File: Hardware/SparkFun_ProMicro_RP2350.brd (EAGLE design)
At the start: 17.8 x 33 mm, 117 parts, among them J2 QWIIC_RIGHT_ANGLE, J5 USB Female Type C Connector, U1 RT9080-33GJ5, U2 RP2350A, U3 WS2812_2020, U4 W25QXX128MBIT, Y1 12MHz

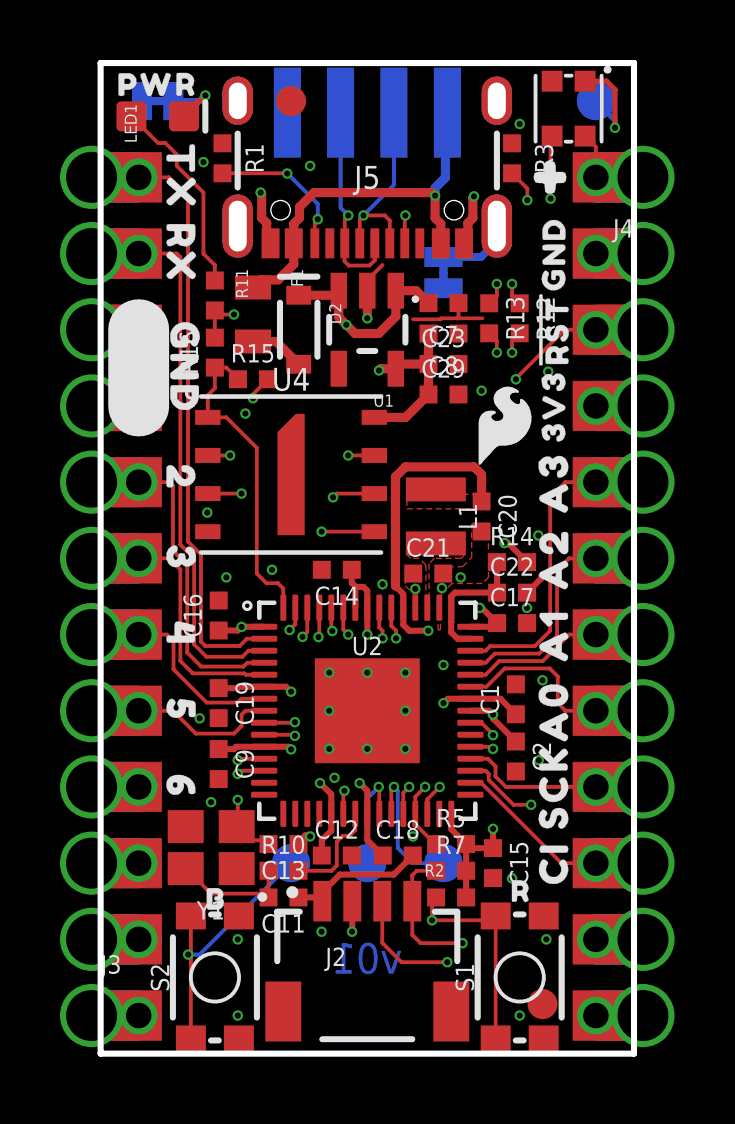
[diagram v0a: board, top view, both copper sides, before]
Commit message: Design review updates
Change all text and labels in schematic to vector font
Fix overlapping text with Qwiic connector in schematic
Add part number to flash memory section title
Fix acid trap on RAW pad
Add more GND vias
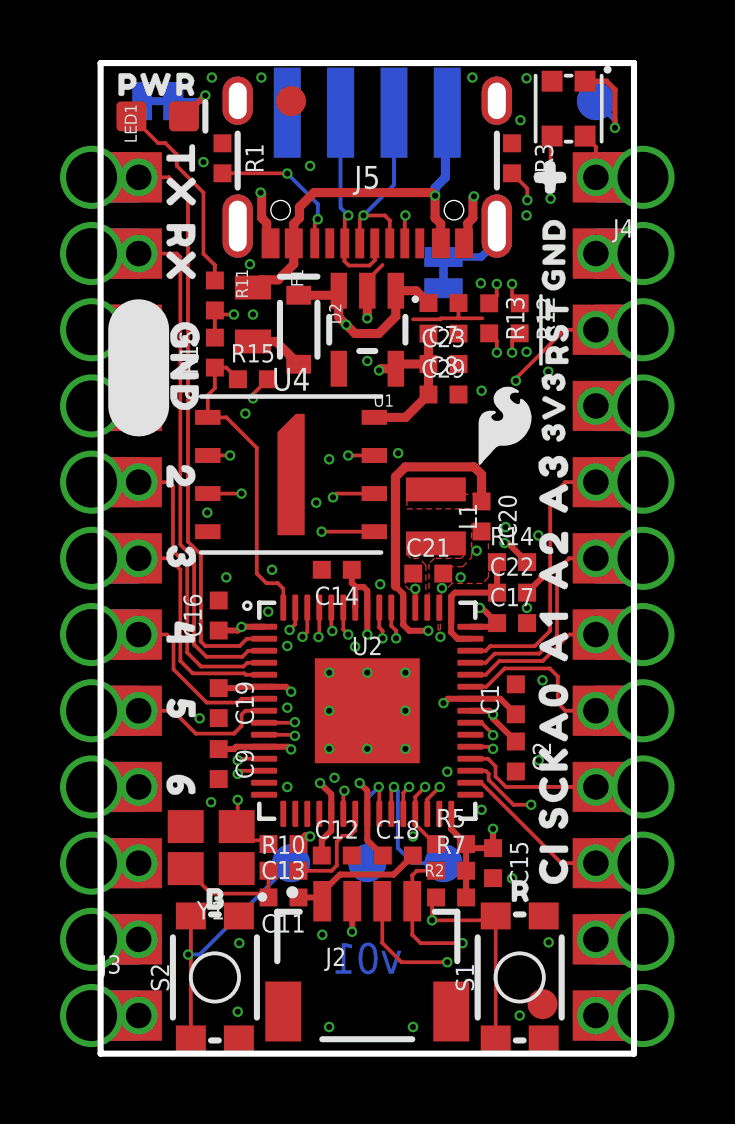
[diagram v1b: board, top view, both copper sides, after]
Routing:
- net GND: vias 39 -> 63
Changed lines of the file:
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@@
 <setting verticaltext="up"/>
 </settings>
-<grid distance="0.05" unitdist="inch" unit="inch" style="lines" multiple="1" display="yes" altdistance="0.005" altunitdist="inch" altunit="inch"/>
+<grid distance="0.05" unitdist="inch" unit="inch" style="lines" multiple="1" display="yes" altdistance="0.001" altunitdist="inch" altunit="inch"/>
 <layers>
 <layer number="1" name="Top" color="4" fill="1" visible="yes" active="yes"/>
@@
 <via x="4.191" y="15.875" extent="1-16" drill="0.2"/>
 <via x="5.715" y="16.129" extent="1-16" drill="0.2"/>
-<via x="9.398" y="15.6464" extent="1-16" drill="0.2"/>
+<via x="9.3218" y="15.6464" extent="1-16" drill="0.2"/>
 <via x="12.0015" y="15.875" extent="1-16" drill="0.2"/>
 <via x="14.9225" y="22.733" extent="1-16" drill="0.2"/>
@@
 <via x="3.429" y="29.718" extent="1-16" drill="0.2"/>
 <via x="6.985" y="29.591" extent="1-16" drill="0.2"/>
-<via x="13.97" y="30.988" extent="1-16" drill="0.2"/>
+<via x="13.9954" y="31.115" extent="1-16" drill="0.2"/>
 <via x="3.556" y="18.034" extent="1-16" drill="0.2"/>
 <via x="7.7978" y="9.1948" extent="1-16" drill="0.2"/>
 <via x="10.414" y="7.239" extent="1-16" drill="0.2"/>
 <via x="6.985" y="7.239" extent="1-16" drill="0.2"/>
-<via x="7.366" y="4.064" extent="1-16" drill="0.2"/>
-<via x="4.572" y="3.81" extent="1-16" drill="0.2"/>
-<via x="4.572" y="1.27" extent="1-16" drill="0.2"/>
-<via x="14.859" y="3.81" extent="1-16" drill="0.2"/>
+<via x="7.3914" y="3.9624" extent="1-16" drill="0.2"/>
+<via x="4.6228" y="3.683" extent="1-16" drill="0.2"/>
+<via x="4.572" y="1.397" extent="1-16" drill="0.2"/>
+<via x="14.9352" y="3.7084" extent="1-16" drill="0.2"/>
 <via x="13.97" y="1.27" extent="1-16" drill="0.2"/>
 <via x="13.716" y="5.842" extent="1-16" drill="0.2"/>
@@
 <wire x1="14.216" y1="15.367" x2="14.6812" y2="15.8322" width="0.2032" layer="1"/>
 <wire x1="14.6812" y1="15.8322" x2="14.6812" y2="15.9258" width="0.2032" layer="1"/>
-<via x="11.43" y="12.954" extent="1-16" drill="0.2"/>
+<via x="11.3284" y="13.8938" extent="1-16" drill="0.2"/>
 <wire x1="11.93" y1="25.019" x2="11.93" y2="24.511" width="0.127" layer="1"/>
 <wire x1="12.7254" y1="24.511" x2="11.93" y2="24.511" width="0.127" layer="1"/>
@@
 <wire x1="11.32995" y1="24.4777" x2="10.414" y2="24.4777" width="0.127" layer="1"/>
 <contactref element="U3" pad="GND"/>
+<via x="12.7" y="8.128" extent="1-16" drill="0.2"/>
+<via x="7.62" y="0.889" extent="1-16" drill="0.2"/>
+<via x="10.414" y="0.889" extent="1-16" drill="0.2"/>
+<via x="6.223" y="13.589" extent="1-16" drill="0.2"/>
+<via x="6.223" y="8.89" extent="1-16" drill="0.2"/>
+<via x="11.557" y="9.398" extent="1-16" drill="0.2"/>
+<via x="8.4836" y="13.5636" extent="1-16" drill="0.2"/>
+<via x="6.223" y="11.5316" extent="1-16" drill="0.2"/>
+<via x="5.588" y="14.732" extent="1-16" drill="0.2"/>
+<via x="7.62" y="19.812" extent="1-16" drill="0.2"/>
+<via x="7.1882" y="18.3642" extent="1-16" drill="0.2"/>
+<via x="5.08" y="24.638" extent="1-16" drill="0.2"/>
+<via x="14.1986" y="32.512" extent="1-16" drill="0.2"/>
+<via x="12.3952" y="32.5374" extent="1-16" drill="0.2"/>
+<via x="5.3594" y="32.5374" extent="1-16" drill="0.2"/>
+<via x="3.7084" y="32.5374" extent="1-16" drill="0.2"/>
+<via x="4.9784" y="26.3144" extent="1-16" drill="0.2"/>
+<via x="12.6746" y="25.6794" extent="1-16" drill="0.2"/>
+<via x="14.1986" y="23.3934" extent="1-16" drill="0.2"/>
+<via x="14.1986" y="27.94" extent="1-16" drill="0.2"/>
+<via x="8.89" y="23.0886" extent="1-16" drill="0.2"/>
+<via x="12.5349" y="16.764" extent="1-16" drill="0.2"/>
+<via x="13.5001" y="17.5514" extent="1-16" drill="0.2"/>
+<via x="9.9187" y="20.0152" extent="1-16" drill="0.2"/>
 </signal>
 <signal name="N$38">
@@
 <wire x1="7.747" y1="29.1641625" x2="8.1865375" y2="29.6037" width="0.3048" layer="15"/>
 <wire x1="18.08" y1="29.21" x2="16.51" y2="29.21" width="0.127" layer="1"/>
-<wire x1="16.1163" y1="29.6037" x2="16.51" y2="29.21" width="0.3048" layer="15"/>
-<wire x1="8.1865375" y1="29.6037" x2="16.1163" y2="29.6037" width="0.3048" layer="15"/>
+<wire x1="15.24" y1="29.21" x2="16.51" y2="29.21" width="0.3048" layer="15"/>
+<wire x1="15.24" y1="29.21" x2="14.8463" y2="29.6037" width="0.3048" layer="15"/>
+<wire x1="8.1865375" y1="29.6037" x2="14.8463" y2="29.6037" width="0.3048" layer="15"/>
 <wire x1="16.51" y1="30.225" x2="16.51" y2="29.21" width="0.127" layer="1"/>
 <wire x1="9.84" y1="25.4301" x2="10.5189" y2="25.4301" width="0.3048" layer="1"/>
@@
 <wire x1="18.08" y1="24.13" x2="16.51" y2="24.13" width="0.127" layer="1"/>
 <wire x1="10.287" y1="8.89" x2="12.1285" y2="10.7315" width="0.127" layer="2"/>
-<wire x1="13.843" y1="22.479" x2="13.843" y2="15.494" width="0.127" layer="2"/>
-<via x="13.843" y="22.479" extent="1-16" drill="0.2"/>
+<wire x1="13.843" y1="22.4282" x2="13.843" y2="15.494" width="0.127" layer="2"/>
+<via x="13.843" y="22.4282" extent="1-16" drill="0.2"/>
 <wire x1="15.468675" y1="24.13" x2="13.843" y2="22.504325" width="0.127" layer="1"/>
-<wire x1="13.843" y1="22.504325" x2="13.843" y2="22.479" width="0.127" layer="1"/>
+<wire x1="13.843" y1="22.504325" x2="13.843" y2="22.4282" width="0.127" layer="1"/>
 <wire x1="15.468675" y1="24.13" x2="16.51" y2="24.13" width="0.127" layer="1"/>
 <contactref element="U2" pad="26"/>
@@
 <contactref element="U4" pad="5"/>
 <via x="7.2644" y="13.8866" extent="1-16" drill="0.2"/>
-<wire x1="7.366" y1="17.399" x2="7.239" y2="17.272" width="0.127" layer="2"/>
-<wire x1="7.239" y1="17.272" x2="7.239" y2="13.912" width="0.127" layer="2"/>
-<wire x1="7.2644" y1="13.8866" x2="7.239" y2="13.912" width="0.127" layer="2"/>
+<wire x1="7.366" y1="17.399" x2="7.366" y2="16.579" width="0.127" layer="2"/>
+<wire x1="7.366" y1="16.579" x2="7.2644" y2="16.4774" width="0.127" layer="2"/>
+<wire x1="7.2644" y1="13.8866" x2="7.2644" y2="16.4774" width="0.127" layer="2"/>
 <via x="7.366" y="17.399" extent="1-16" drill="0.2"/>
 <wire x1="7.366" y1="17.399" x2="9.125" y2="17.399" width="0.127" layer="1"/>

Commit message: DFM adjustments
Nudge C1 away from C2
Nudge C20 away from L1
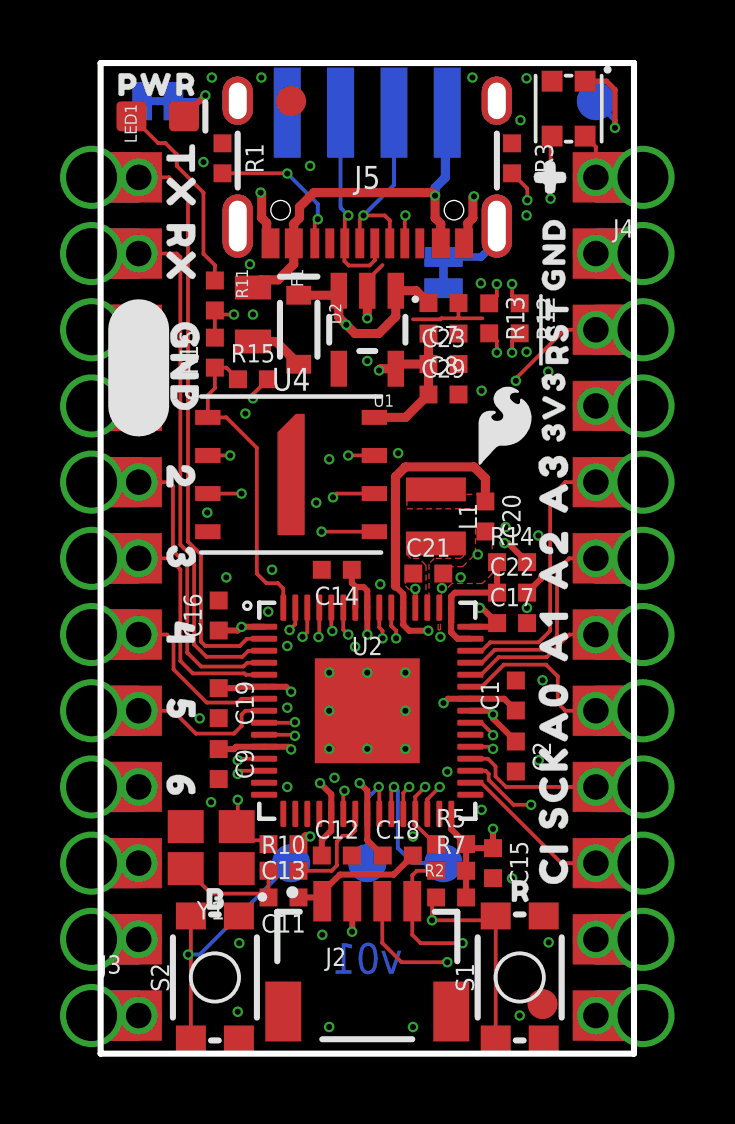
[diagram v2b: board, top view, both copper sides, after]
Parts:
- moved C1 0.13 mm to (13.8, 11.9)
- moved C20 0.13 mm to (12.8, 17.9)
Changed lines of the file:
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@@
 <setting verticaltext="up"/>
 </settings>
-<grid distance="0.05" unitdist="inch" unit="inch" style="lines" multiple="1" display="yes" altdistance="0.001" altunitdist="inch" altunit="inch"/>
+<grid distance="0.05" unitdist="inch" unit="inch" style="lines" multiple="1" display="yes" altdistance="0.005" altunitdist="inch" altunit="inch"/>
 <layers>
 <layer number="1" name="Top" color="4" fill="1" visible="yes" active="yes"/>
@@
 <attribute name="VALUE" x="12.392" y="24.511" size="0.6096" layer="27" font="vector" ratio="20" rot="R270" align="top-center"/>
 </element>
-<element name="C20" library="SparkFun-Capacitors" package="0402-TIGHT" value="10uF" x="12.7" y="17.907" smashed="yes" rot="R270">
-<attribute name="NAME" x="13.262" y="17.907" size="0.6096" layer="25" font="vector" ratio="20" rot="R270" align="bottom-center"/>
-<attribute name="PROD_ID" value="CAP-14848" x="-29.21" y="20.447" size="1.778" layer="27" font="vector" ratio="15" rot="R270" display="off"/>
-<attribute name="VALUE" value="10uF" x="12.138" y="17.907" size="0.6096" layer="27" font="vector" ratio="20" rot="R270" align="top-center"/>
+<element name="C20" library="SparkFun-Capacitors" package="0402-TIGHT" value="10uF" x="12.827" y="17.907" smashed="yes" rot="R270">
+<attribute name="NAME" x="13.389" y="17.907" size="0.6096" layer="25" font="vector" ratio="20" rot="R270" align="bottom-center"/>
+<attribute name="PROD_ID" value="CAP-14848" x="-29.083" y="20.447" size="1.778" layer="27" font="vector" ratio="15" rot="R270" display="off"/>
+<attribute name="VALUE" value="10uF" x="12.265" y="17.907" size="0.6096" layer="27" font="vector" ratio="20" rot="R270" align="top-center"/>
 </element>
 <element name="C21" library="SparkFun-Capacitors" package="0402-TIGHT" value="10uF" x="10.922" y="16.002" smashed="yes">
@@
 <attribute name="VALUE" x="8.89" y="9.13" size="0.6096" layer="27" align="center"/>
 </element>
-<element name="C1" library="SparkFun-Capacitors" package="0402-TIGHT" value="0.1uF" x="13.843" y="11.811" smashed="yes" rot="R90">
-<attribute name="NAME" x="13.281" y="11.811" size="0.6096" layer="25" font="vector" ratio="20" rot="R90" align="bottom-center"/>
-<attribute name="PROD_ID" value="CAP-14993" x="13.843" y="13.081" size="1.778" layer="27" font="vector" ratio="15" rot="R90" display="off"/>
-<attribute name="VALUE" x="14.405" y="11.811" size="0.6096" layer="27" font="vector" ratio="20" rot="R90" align="top-center"/>
+<element name="C1" library="SparkFun-Capacitors" package="0402-TIGHT" value="0.1uF" x="13.843" y="11.938" smashed="yes" rot="R90">
+<attribute name="NAME" x="13.281" y="11.938" size="0.6096" layer="25" font="vector" ratio="20" rot="R90" align="bottom-center"/>
+<attribute name="PROD_ID" value="CAP-14993" x="13.843" y="13.208" size="1.778" layer="27" font="vector" ratio="15" rot="R90" display="off"/>
+<attribute name="VALUE" x="14.405" y="11.938" size="0.6096" layer="27" font="vector" ratio="20" rot="R90" align="top-center"/>
 </element>
 <element name="L1" library="SparkFun-Coils" package="1008(2520)" value="4.7μH" x="11.176" y="17.907" smashed="yes" rot="R270">
@@
 <vertex x="11.2522" y="16.2306"/>
 <vertex x="12.065" y="16.2306"/>
-<vertex x="12.3698" y="16.5354"/>
-<vertex x="12.3698" y="17.653"/>
-<vertex x="12.9286" y="17.653"/>
-<vertex x="12.9286" y="15.875"/>
+<vertex x="12.4968" y="16.6624"/>
+<vertex x="12.4968" y="17.653"/>
+<vertex x="13.0556" y="17.653"/>
+<vertex x="13.0556" y="16.002"/>
 <vertex x="12.7254" y="15.6718"/>
 <vertex x="11.7094" y="15.6718"/>
@@
 <via x="14.1986" y="27.94" extent="1-16" drill="0.2"/>
 <via x="8.89" y="23.0886" extent="1-16" drill="0.2"/>
-<via x="12.5349" y="16.764" extent="1-16" drill="0.2"/>
+<via x="12.573" y="16.637" extent="1-16" drill="0.2"/>
 <via x="13.5001" y="17.5514" extent="1-16" drill="0.2"/>
 <via x="9.9187" y="20.0152" extent="1-16" drill="0.2"/>
@@
 <wire x1="18.08" y1="19.05" x2="16.51" y2="19.05" width="0.127" layer="1"/>
 <contactref element="U2" pad="43"/>
-<wire x1="14.4714" y1="13.5824" x2="12.9869" y2="13.5824" width="0.127" layer="1"/>
-<wire x1="12.9869" y1="13.5824" x2="12.8345" y2="13.43" width="0.127" layer="1"/>
-<wire x1="12.3265" y1="13.43" x2="12.8345" y2="13.43" width="0.127" layer="1"/>
-<wire x1="14.4714" y1="13.5824" x2="14.986" y2="14.097" width="0.127" layer="1"/>
+<wire x1="14.5984" y1="13.7094" x2="12.9869" y2="13.7094" width="0.127" layer="1"/>
+<wire x1="12.9869" y1="13.7094" x2="12.7075" y2="13.43" width="0.127" layer="1"/>
+<wire x1="12.3265" y1="13.43" x2="12.7075" y2="13.43" width="0.127" layer="1"/>
+<wire x1="14.5984" y1="13.7094" x2="14.986" y2="14.097" width="0.127" layer="1"/>
 </signal>
 <signal name="A2">
@@
 <wire x1="18.08" y1="16.51" x2="16.51" y2="16.51" width="0.127" layer="1"/>
 <contactref element="U2" pad="42"/>
-<wire x1="14.62329375" y1="13.3348" x2="13.1393" y2="13.3348" width="0.127" layer="1"/>
-<wire x1="13.1393" y1="13.3348" x2="12.8345" y2="13.03" width="0.127" layer="1"/>
-<wire x1="12.3265" y1="13.03" x2="12.8345" y2="13.03" width="0.127" layer="1"/>
-<wire x1="14.62329375" y1="13.3348" x2="15.2146" y2="13.92610625" width="0.127" layer="1"/>
+<wire x1="14.75029375" y1="13.4618" x2="13.1393" y2="13.4618" width="0.127" layer="1"/>
+<wire x1="13.1393" y1="13.4618" x2="12.7075" y2="13.03" width="0.127" layer="1"/>
+<wire x1="12.3265" y1="13.03" x2="12.7075" y2="13.03" width="0.127" layer="1"/>
+<wire x1="14.75029375" y1="13.4618" x2="15.2146" y2="13.92610625" width="0.127" layer="1"/>
 </signal>
 <signal name="A1">
@@
 <contactref element="J4" pad="7B"/>
 <wire x1="16.51" y1="13.97" x2="15.621" y2="13.97" width="0.127" layer="1"/>
-<wire x1="15.621" y1="13.97" x2="14.7382" y2="13.0872" width="0.127" layer="1"/>
-<wire x1="14.7382" y1="13.0872" x2="13.2917" y2="13.0872" width="0.127" layer="1"/>
-<wire x1="13.2917" y1="13.0872" x2="12.8345" y2="12.63" width="0.127" layer="1"/>
-<wire x1="12.8345" y1="12.63" x2="12.3265" y2="12.63" width="0.127" layer="1"/>
+<wire x1="15.621" y1="13.97" x2="14.8652" y2="13.2142" width="0.127" layer="1"/>
+<wire x1="14.8652" y1="13.2142" x2="13.2663" y2="13.2142" width="0.127" layer="1"/>
+<wire x1="13.2663" y1="13.2142" x2="12.6821" y2="12.63" width="0.127" layer="1"/>
+<wire x1="12.6821" y1="12.63" x2="12.3265" y2="12.63" width="0.127" layer="1"/>
 <wire x1="18.08" y1="13.97" x2="16.51" y2="13.97" width="0.127" layer="1"/>
 <contactref element="U2" pad="41"/>
@@
 <wire x1="18.08" y1="11.43" x2="16.51" y2="11.43" width="0.127" layer="1"/>
 <contactref element="U2" pad="40"/>
-<wire x1="14.9734" y1="12.8396" x2="13.4695" y2="12.8396" width="0.127" layer="1"/>
-<wire x1="12.3265" y1="12.23" x2="12.8599" y2="12.23" width="0.127" layer="1"/>
-<wire x1="13.4695" y1="12.8396" x2="12.8599" y2="12.23" width="0.127" layer="1"/>
+<wire x1="14.8464" y1="12.9666" x2="13.4441" y2="12.9666" width="0.127" layer="1"/>
+<wire x1="12.3265" y1="12.23" x2="12.7075" y2="12.23" width="0.127" layer="1"/>
+<wire x1="13.4441" y1="12.9666" x2="12.7075" y2="12.23" width="0.127" layer="1"/>
 <wire x1="15.24" y1="12.573" x2="15.24" y2="11.684" width="0.127" layer="1"/>
 <wire x1="15.494" y1="11.43" x2="16.51" y2="11.43" width="0.127" layer="1"/>
 <wire x1="15.494" y1="11.43" x2="15.24" y2="11.684" width="0.127" layer="1"/>
-<wire x1="15.24" y1="12.573" x2="14.9734" y2="12.8396" width="0.127" layer="1"/>
+<wire x1="15.24" y1="12.573" x2="14.8464" y2="12.9666" width="0.127" layer="1"/>
 </signal>
 <signal name="1/RX0">
@@
 <wire x1="11.43" y1="11.684" x2="10.922" y2="12.192" width="0.2032" layer="2"/>
 <contactref element="C1" pad="1"/>
-<wire x1="13.843" y1="11.311" x2="13.324" y2="11.83" width="0.2032" layer="1"/>
-<wire x1="13.324" y1="11.83" x2="12.3265" y2="11.83" width="0.2032" layer="1"/>
+<wire x1="13.843" y1="11.438" x2="13.451" y2="11.83" width="0.2032" layer="1"/>
+<wire x1="13.451" y1="11.83" x2="12.3265" y2="11.83" width="0.2032" layer="1"/>
 <contactref element="L1" pad="1"/>
 <wire x1="10.09" y1="14.8665" x2="10.09" y2="15.3187375" width="0.2032" layer="1"/>
@@
 <wire x1="9.8298" y1="15.5789375" x2="9.8298" y2="19.2278" width="0.3048" layer="1"/>
 <wire x1="10.16" y1="19.558" x2="12.446" y2="19.558" width="0.3048" layer="1"/>
-<wire x1="12.7" y1="18.407" x2="12.7" y2="19.304" width="0.3048" layer="1"/>
-<wire x1="12.7" y1="19.304" x2="12.446" y2="19.558" width="0.3048" layer="1"/>
+<wire x1="12.827" y1="18.407" x2="12.827" y2="19.177" width="0.3048" layer="1"/>
+<wire x1="12.827" y1="19.177" x2="12.446" y2="19.558" width="0.3048" layer="1"/>
 <polygon width="0.127" layer="1" isolate="0.127" thermals="no">
 <vertex x="10.2108" y="19.1008"/>
 <vertex x="10.2108" y="18.161"/>
-<vertex x="12.9032" y="18.161"/>
-<vertex x="12.9032" y="18.6436"/>
+<vertex x="13.0302" y="18.161"/>
+<vertex x="13.0302" y="18.6436"/>
 <vertex x="12.0396" y="18.6436"/>
 <vertex x="12.0396" y="19.1008"/>

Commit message: Improve button silk
Remove "B" silk label from boot button
Increase size of "R" silk label for reset button
Add "BOOT" and "RST" silk to bottom with button symbols
Move Qwiic logo and test point labels up
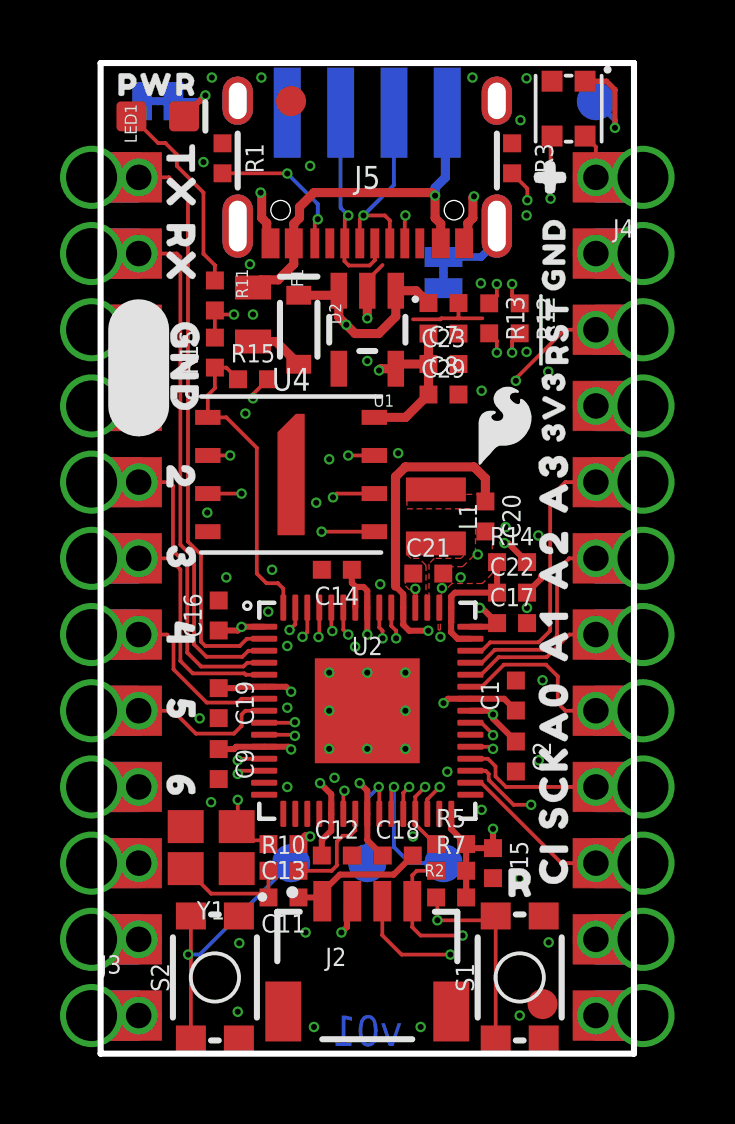
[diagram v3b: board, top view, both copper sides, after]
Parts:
- added U$41: (no value), output:BOOT0
- U$44: device output:B1 -> output:RST0
- moved U$44 8.61 mm to (12.1, 2.54), flipped to the bottom
- moved LOGO3 3.18 mm to (8.89, 4.45)
- moved U$18 2.67 mm to (8.76, 7.62)
- moved U$35 2.67 mm to (11.3, 7.62)
- moved U$38 2.67 mm to (6.22, 7.62)
- moved U$37 0.28 mm to (14.0, 5.69)
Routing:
- net 17/SCL: track 11.2 -> 10.7 mm
